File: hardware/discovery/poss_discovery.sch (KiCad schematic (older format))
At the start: 28 parts, among them SW1 SW_PUSH, SW10 SW_PUSH, SW11 SW_PUSH, SW12 SW_PUSH, SW13 SW_PUSH, SW14 SW_PUSH, SW15 SW_PUSH, SW16 SW_PUSH, SW17 SW_PUSH, SW18 SW_PUSH, SW19 SW_PUSH, SW2 SW_PUSH, SW20 SW_PUSH, SW21 SW_PUSH, SW22 SW_PUSH, SW3 SW_PUSH, SW4 SW_PUSH, SW5 SW_PUSH, SW6 SW_PUSH, SW7 SW_PUSH, SW8 SW_PUSH, SW9 SW_PUSH, U1 STM32F4_DISCO_Header

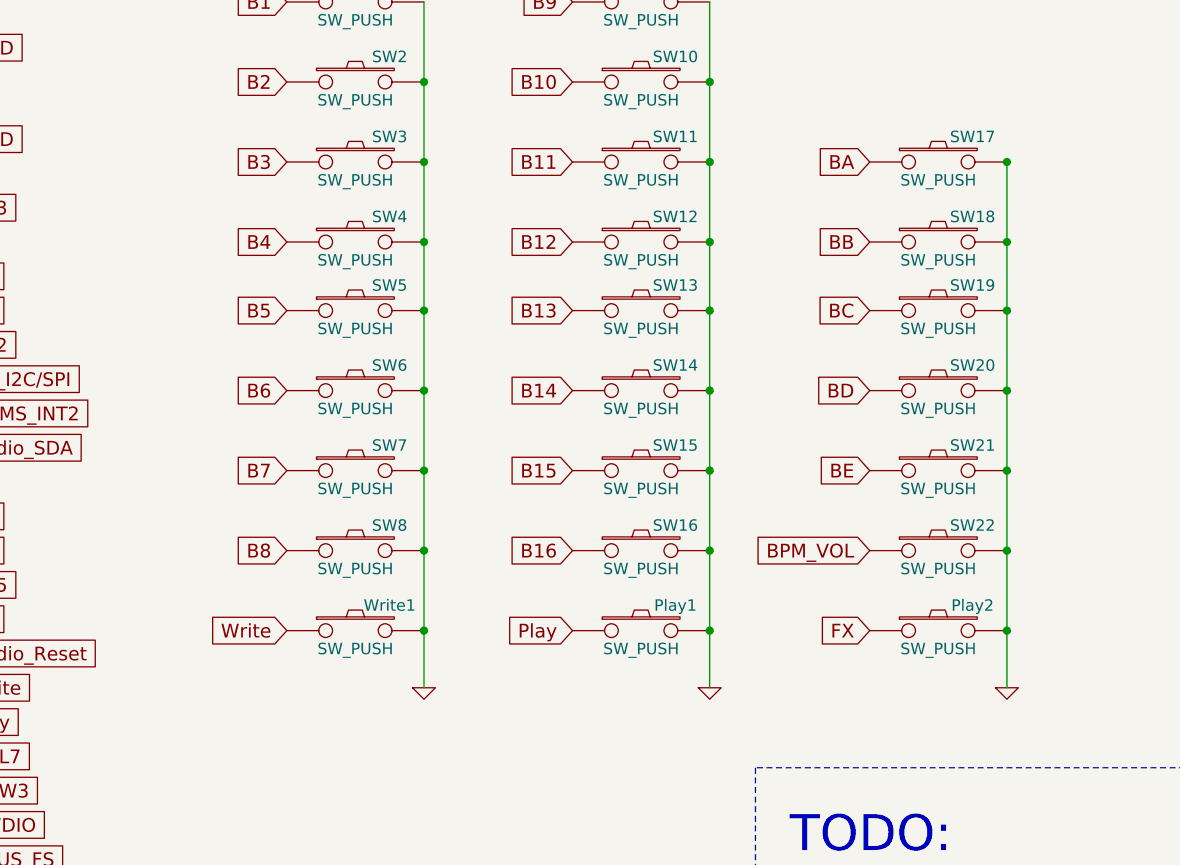
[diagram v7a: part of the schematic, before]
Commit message: Discovery: Connect all button to the wakeup pin
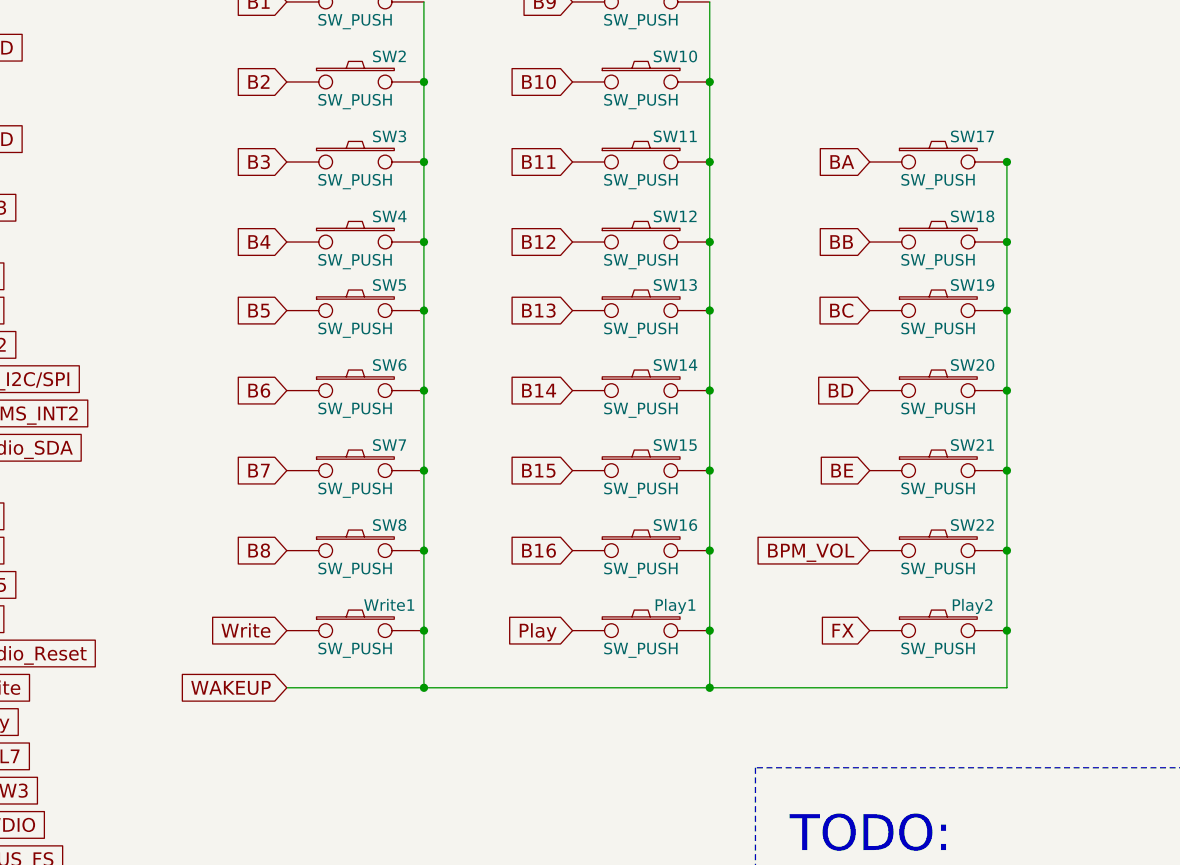
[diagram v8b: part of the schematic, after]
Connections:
- net GND: no longer Play1.2, Play2.2, SW1.2, SW10.2, SW11.2, SW12.2, SW13.2, SW14.2, SW15.2, SW16.2, SW17.2, SW18.2, SW19.2, SW2.2, SW20.2, SW21.2, SW22.2, SW3.2, SW4.2, SW5.2, SW6.2, SW7.2, SW8.2, SW9.2, Write1.2
- new net WAKEUP: Play1.2, Play2.2, SW1.2, SW10.2, SW11.2, SW12.2, SW13.2, SW14.2, SW15.2, SW16.2, SW17.2, SW18.2, SW19.2, SW2.2, SW20.2, SW21.2, SW22.2, SW3.2, SW4.2, SW5.2, SW6.2, SW7.2, SW8.2, SW9.2, Write1.2
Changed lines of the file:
@@
 	1    0    0    -1
 $EndComp
-Wire Wire Line
-	7400 750  7400 3750
-Connection ~ 7400 3150
-Connection ~ 7400 2800
-Connection ~ 7400 2450
-Connection ~ 7400 2100
-Connection ~ 7400 1800
-Connection ~ 7400 1450
-Connection ~ 7400 1100
-Wire Wire Line
-	8650 750  8650 3750
-Connection ~ 8650 3150
-Connection ~ 8650 2800
-Connection ~ 8650 2450
-Connection ~ 8650 2100
-Connection ~ 8650 1800
-Connection ~ 8650 1450
-Connection ~ 8650 1100
-Wire Wire Line
-	9950 1450 9950 3750
-Connection ~ 9950 3150
-Connection ~ 9950 2800
-Connection ~ 9950 2450
-Connection ~ 9950 2100
-Connection ~ 9950 1800
-Connection ~ 9950 1450
 $Comp
 L POT-RESCUE-poss_discovery RV2
@@
 	1    0    0    -1
 $EndComp
-Wire Wire Line
-	4850 5900 4950 5900
-Wire Wire Line
-	4700 5750 4700 5650
-Wire Wire Line
-	4550 5900 4450 5900
 $Comp
 L POT-RESCUE-poss_discovery RV1
@@
 	1    0    0    -1
 $EndComp
-Wire Wire Line
-	3500 5900 3600 5900
-Wire Wire Line
-	3350 5750 3350 5650
-Wire Wire Line
-	3200 5900 3100 5900
 $Comp
 L STM32F4_DISCO_Header U1
@@
 Text GLabel 4450 5900 0    60   Input ~ 0
 3V3
-$Comp
-L GND #PWR01
-U 1 1 585CFBB5
-P 9950 3750
-F 0 "#PWR01" H 9950 3750 30  0001 C CNN
-F 1 "GND" H 9950 3680 30  0001 C CNN
-F 2 "" H 9950 3750 60  0001 C CNN
-F 3 "" H 9950 3750 60  0001 C CNN
-	1    9950 3750
-	1    0    0    -1
-$EndComp
-Connection ~ 9950 3500
 Text GLabel 2200 1350 2    60   Input ~ 0
 GND
@@
 $EndSheet
 $Comp
-L GND #PWR02
-U 1 1 585D97BE
-P 8650 3750
-F 0 "#PWR02" H 8650 3750 30  0001 C CNN
-F 1 "GND" H 8650 3680 30  0001 C CNN
-F 2 "" H 8650 3750 60  0001 C CNN
-F 3 "" H 8650 3750 60  0001 C CNN
-	1    8650 3750
-	1    0    0    -1
-$EndComp
-Connection ~ 8650 3500
-$Comp
-L GND #PWR03
-U 1 1 585D9E6B
-P 7400 3750
-F 0 "#PWR03" H 7400 3750 30  0001 C CNN
-F 1 "GND" H 7400 3680 30  0001 C CNN
-F 2 "" H 7400 3750 60  0001 C CNN
-F 3 "" H 7400 3750 60  0001 C CNN
-	1    7400 3750
-	1    0    0    -1
-$EndComp
-Connection ~ 7400 3500
-$Comp
-L GND #PWR04
+L GND #PWR01
 U 1 1 585DAFE1
 P 4950 6000
-F 0 "#PWR04" H 4950 6000 30  0001 C CNN
+F 0 "#PWR01" H 4950 6000 30  0001 C CNN
 F 1 "GND" H 4950 5930 30  0001 C CNN
 F 2 "" H 4950 6000 60  0001 C CNN
@@
 $EndComp
 $Comp
-L GND #PWR05
+L GND #PWR02
 U 1 1 585DB05F
 P 3600 6000
-F 0 "#PWR05" H 3600 6000 30  0001 C CNN
+F 0 "#PWR02" H 3600 6000 30  0001 C CNN
 F 1 "GND" H 3600 5930 30  0001 C CNN
 F 2 "" H 3600 6000 60  0001 C CNN
@@
 	1    0    0    -1
 $EndComp
-Wire Wire Line
-	3600 5900 3600 6000
-Wire Wire Line
-	4950 5900 4950 6000
-Wire Wire Line
-	5350 4950 5500 4950
-Wire Wire Line
-	5500 4950 5500 5100
 Text GLabel 5500 4950 2    60   Input ~ 0
 GND
 $Comp
-L GND #PWR06
+L GND #PWR03
 U 1 1 585DBA46
 P 5500 5100
-F 0 "#PWR06" H 5500 5100 30  0001 C CNN
+F 0 "#PWR03" H 5500 5100 30  0001 C CNN
 F 1 "GND" H 5500 5030 30  0001 C CNN
 F 2 "" H 5500 5100 60  0001 C CNN
@@
 Text Notes 9000 5500 0    157  ~ 0
 TODO:\n - Debug port\n - Encoders\n - VBAT sensing\n -
+Wire Wire Line
+	7400 750  7400 3750
+Connection ~ 7400 3150
+Connection ~ 7400 2800
+Connection ~ 7400 2450
+Connection ~ 7400 2100
+Connection ~ 7400 1800
+Connection ~ 7400 1450
+Connection ~ 7400 1100
+Wire Wire Line
+	8650 750  8650 3750
+Connection ~ 8650 3150
+Connection ~ 8650 2800
+Connection ~ 8650 2450
+Connection ~ 8650 2100
+Connection ~ 8650 1800
+Connection ~ 8650 1450
+Connection ~ 8650 1100
+Wire Wire Line
+	9950 3750 9950 1450
+Connection ~ 9950 3150
+Connection ~ 9950 2800
+Connection ~ 9950 2450
+Connection ~ 9950 2100
+Connection ~ 9950 1800
+Connection ~ 9950 1450
+Wire Wire Line
+	4850 5900 4950 5900
+Wire Wire Line
+	4700 5750 4700 5650
+Wire Wire Line
+	4550 5900 4450 5900
+Wire Wire Line
+	3500 5900 3600 5900
+Wire Wire Line
+	3350 5750 3350 5650
+Wire Wire Line
+	3200 5900 3100 5900
+Connection ~ 9950 3500
+Connection ~ 8650 3500
+Connection ~ 7400 3500
+Wire Wire Line
+	3600 5900 3600 6000
+Wire Wire Line
+	4950 5900 4950 6000
+Wire Wire Line
+	5350 4950 5500 4950
+Wire Wire Line
+	5500 4950 5500 5100
 Wire Notes Line
 	11150 4100 8850 4100
 Wire Notes Line
 	8850 4100 8850 6450
+Wire Wire Line
+	6800 3750 9950 3750
+Connection ~ 8650 3750
+Connection ~ 7400 3750
+Text GLabel 6800 3750 0    60   Input ~ 0
+WAKEUP
 $EndSCHEMATC
